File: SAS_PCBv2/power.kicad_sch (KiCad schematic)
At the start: 15 parts, among them J3 Conn_01x02_Pin, Q2 AO3401A, Q3 AO3401A, SW1 SW_SPST, U2 LF33_TO220

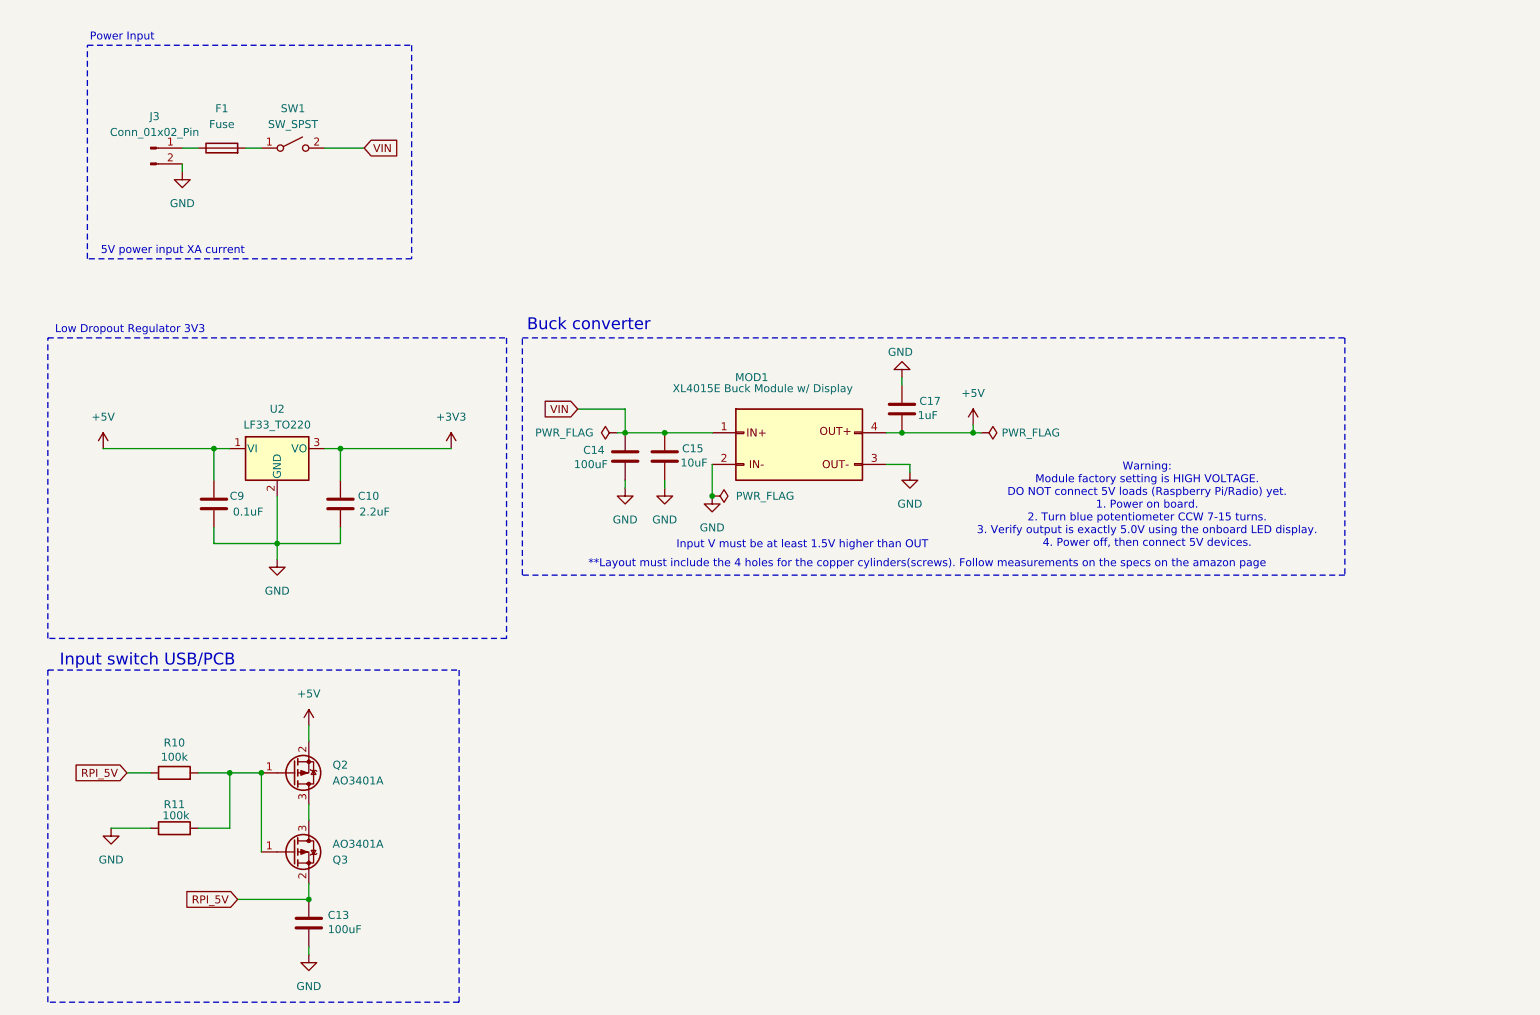
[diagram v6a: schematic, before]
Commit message: Amélioration des modèles Rpi et page power, switch PCB/USB fonctionnelle
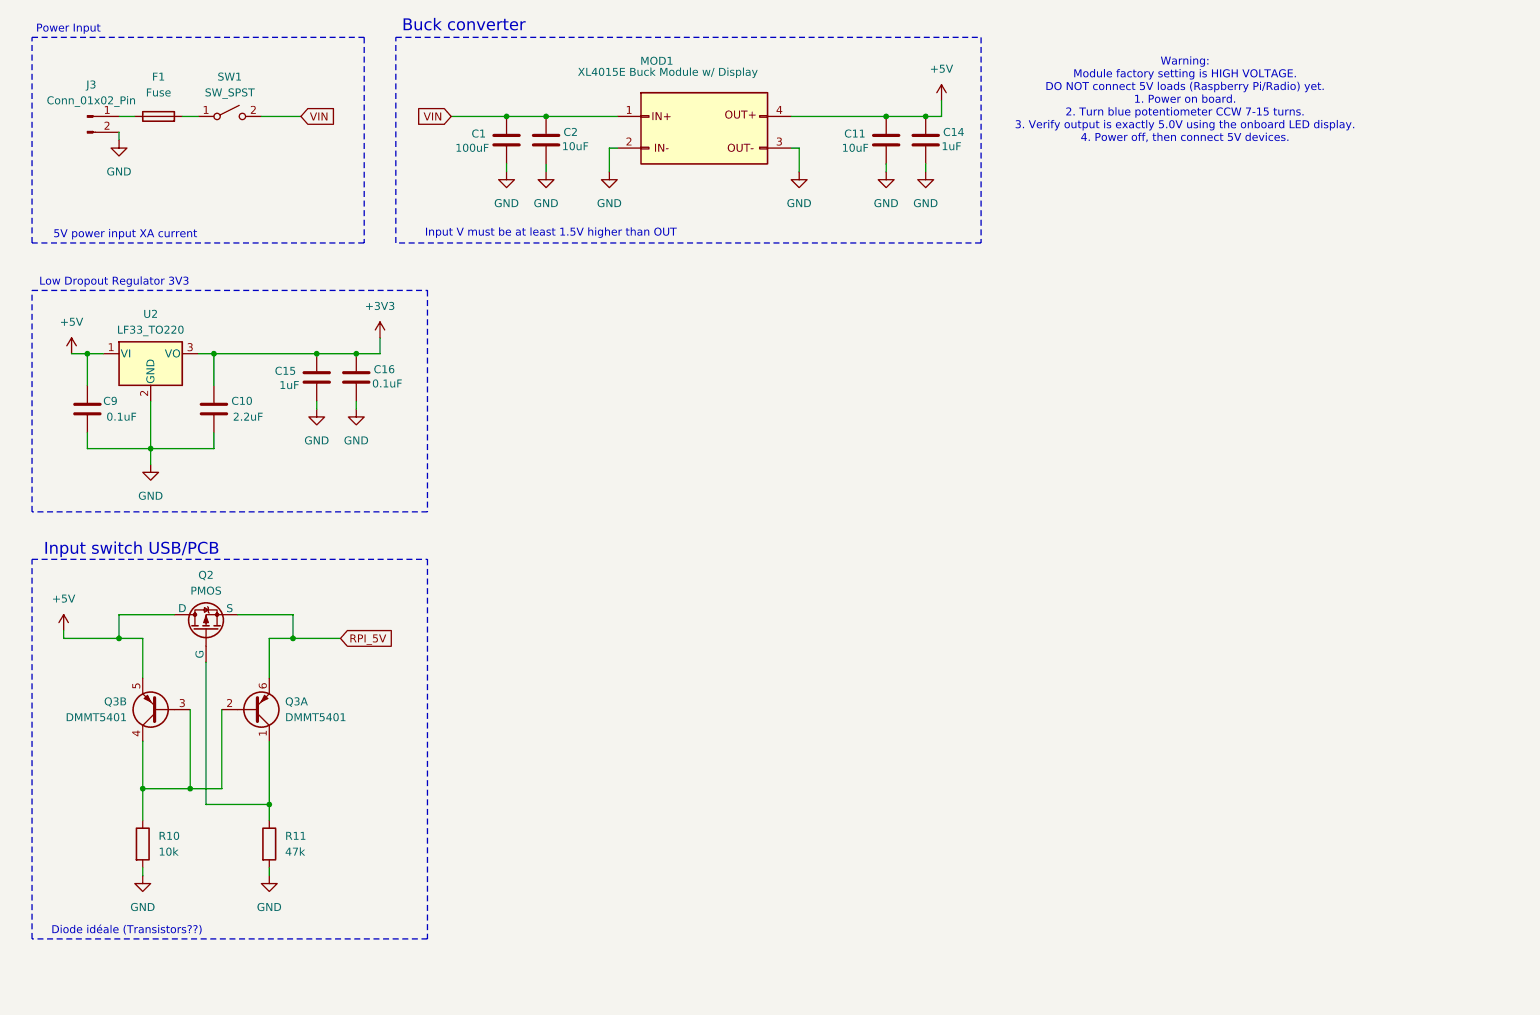
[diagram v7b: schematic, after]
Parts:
- removed C13: 100uF, symbol Device:C
- removed C17: 1uF, symbol Device:C
- removed Q2, Q3: AO3401A, Package_TO_SOT_SMD:SOT-23, symbol Transistor_FET:AO3401A
- added C1: 100uF, symbol Device:C
- added C11, C2: 10uF, symbol Device:C
- added C16: 0.1uF, symbol Device:C
- added Q2: PMOS, symbol Simulation_SPICE:PMOS
- added Q3: DMMT5401, Package_TO_SOT_SMD:SOT-23-6, symbol Transistor_BJT:DMMT5401
- C14: value 100uF -> 1uF
- C15: value 10uF -> 1uF
- R10: value 100k -> 10k
- R11: value 100k -> 47k
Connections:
- net +3V3: now also C15.1, C16.1
- net +5V: now also C14.1, C11.1, Q2.1 (D), Q3.5 (E2)
- net GND: now also R10.2, R11.2, C1.2, C11.2, C16.2, C2.2; no longer R11.1
- net RPI_5V: now also Q2.3 (S), Q3.6 (E1); no longer R10.1
- net VIN: now also C1.1, C2.1; no longer C14.1, C15.1
- new net: Q3.2 (B1), Q3.3 (B2), Q3.4 (C2), R10.1
- new net: Q2.2 (G), Q3.1 (C1), R11.1
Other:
- note added: "Diode idéale (Transistors??)"
- note removed: "**Layout must include the 4 holes for the copper cylinders(screws). Follow measurements on the specs on the amazon page"
- moved on the sheet: C10, C9, F1, J3, MOD1, SW1, U2

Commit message: Identification des transistors, footprint BMP280 et GPS Neo-6M, correction du fan PWM
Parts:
- removed Q2: PMOS, symbol Simulation_SPICE:PMOS
- removed Q3: DMMT5401, Package_TO_SOT_SMD:SOT-23-6, symbol Transistor_BJT:DMMT5401
- added MOSFET1: FQPF47P06, SAS_PCBv2_footprint:PMOS_FQP_ONS, symbol SAS_PCBv2_symbol:FQPF47P06
- added Q2, Q3: 2N4403, SAS_PCBv2_footprint:PBIP_2N4403_DIO, symbol Simulation_SPICE:PNP
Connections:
- net +5V: now also MOSFET1.2 (D), Q3.3 (E)
- net RPI_5V: now also MOSFET1.3 (S), Q2.3 (E)
- net at R10.1: now also Q2.2 (B), Q3.1 (C), Q3.2 (B)
- net at R11.1: now also MOSFET1.1 (G), Q2.1 (C)
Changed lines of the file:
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@@
-	)
-	(symbol
-		(lib_id "Transistor_BJT:DMMT5401")
-		(at 38.1 128.27 180)
-		(unit 2)
-		(exclude_from_sim no)
-		(in_bom yes)
-		(on_board yes)
-		(dnp no)
-		(fields_autoplaced yes)
-		(property "Reference" "Q3"
-			(at 33.02 126.9999 0)
-			(effects
-				(font
-					(size 1.27 1.27)
-				)
-				(justify left)
-			)
-		)
-		(property "Value" "DMMT5401"
-			(at 33.02 129.5399 0)
-			(effects
-				(font
-					(size 1.27 1.27)
-				)
-				(justify left)
-			)
-		)
-		(property "Footprint" "Package_TO_SOT_SMD:SOT-23-6"
-			(at 33.02 130.81 0)
-			(effects
-				(font
-					(size 1.27 1.27)
-				)
-				(hide yes)
-			)
-		)
-		(property "Datasheet" "https://www.diodes.com/assets/Datasheets/ds30437.pdf"
-			(at 38.1 128.27 0)
-			(effects
-				(font
-					(size 1.27 1.27)
-				)
-				(hide yes)
-			)
-		)
-		(property "Description" "Dual PNP transistor, 6 pin package"
-			(at 38.1 128.27 0)
-			(effects
-				(font
-					(size 1.27 1.27)
-				)
-				(hide yes)
-			)
-		)
-		(pin "4"
-		)
-		(pin "5"
-		)
-		(pin "6"
-		)
-		(pin "2"
-		)
-		(pin "3"
-		)
-		(pin "1"
-		)
-		(instances
-			(project ""
-				(path "/9d66b581-dc57-43dc-b827-73e5c0cd12f6/3d73fe98-5b95-4bdf-b7ce-5bce46366f48"
-					(reference "Q3")
-					(unit 2)
-				)
-			)
-		)
 	)
 	(symbol
@@
 	)
 	(symbol
+		(lib_id "Simulation_SPICE:PNP")
+		(at 38.1 128.27 180)
+		(unit 1)
+		(exclude_from_sim no)
+		(in_bom yes)
+		(on_board yes)
+		(dnp no)
+		(property "Reference" "Q3"
+			(at 33.02 126.9999 0)
+			(effects
+				(font
+					(size 1.27 1.27)
+				)
+				(justify left)
+			)
+		)
+		(property "Value" "2N4403"
+			(at 33.02 129.5399 0)
+			(effects
+				(font
+					(size 1.27 1.27)
+				)
+				(justify left)
+			)
+		)
+		(property "Footprint" "SAS_PCBv2_footprint:PBIP_2N4403_DIO"
+			(at 2.54 128.27 0)
+			(effects
+				(font
+					(size 1.27 1.27)
+				)
+				(hide yes)
+			)
+		)
+		(property "Datasheet" "https://diotec.com/request/datasheet/2n4403.pdf"
+			(at 2.54 128.27 0)
+			(effects
+				(font
+					(size 1.27 1.27)
+				)
+				(hide yes)
+			)
+		)
+		(property "Description" "2N4403"
+			(at 38.1 128.27 0)
+			(effects
+				(font
+					(size 1.27 1.27)
+				)
+				(hide yes)
+			)
+		)
+		(property "Sim.Device" "PNP"
+			(at 38.1 128.27 0)
+			(effects
+				(font
+					(size 1.27 1.27)
+				)
+				(hide yes)
+			)
+		)
+		(property "Sim.Type" "GUMMELPOON"
+			(at 38.1 128.27 0)
+			(effects
+				(font
+					(size 1.27 1.27)
+				)
+				(hide yes)
+			)
+		)
+		(property "Sim.Pins" "1=C 2=B 3=E"
+			(at 38.1 128.27 0)
+			(effects
+				(font
+					(size 1.27 1.27)
+				)
+				(hide yes)
+			)
+		)
+		(pin "3"
+		)
+		(pin "2"
+		)
+		(pin "1"
+		)
+		(instances
+			(project "SAS_PCBv2"
+				(path "/9d66b581-dc57-43dc-b827-73e5c0cd12f6/3d73fe98-5b95-4bdf-b7ce-5bce46366f48"
+					(reference "Q3")
+					(unit 1)
+				)
+			)
+		)
+	)
+	(symbol
 		(lib_id "power:GND")
 		(at 110.49 41.91 0)
@@
 	)
 	(symbol
-		(lib_id "Simulation_SPICE:PMOS")
-		(at 45.72 115.57 90)
-		(unit 1)
-		(exclude_from_sim no)
-		(in_bom yes)
-		(on_board yes)
-		(dnp no)
-		(fields_autoplaced yes)
-		(property "Reference" "Q2"
-			(at 45.72 106.68 90)
-			(effects
-				(font
-					(size 1.27 1.27)
-				)
-			)
-		)
-		(property "Value" "PMOS"
-			(at 45.72 109.22 90)
-			(effects
-				(font
-					(size 1.27 1.27)
-				)
-			)
-		)
-		(property "Footprint" ""
-			(at 43.18 110.49 0)
-			(effects
-				(font
-					(size 1.27 1.27)
-				)
-				(hide yes)
-			)
-		)
-		(property "Datasheet" "https://ngspice.sourceforge.io/docs/ngspice-html-manual/manual.xhtml#cha_MOSFETs"
-			(at 58.42 115.57 0)
-			(effects
-				(font
-					(size 1.27 1.27)
-				)
-				(hide yes)
-			)
-		)
-		(property "Description" "P-MOSFET transistor, drain/source/gate"
-			(at 45.72 115.57 0)
-			(effects
-				(font
-					(size 1.27 1.27)
-				)
-				(hide yes)
-			)
-		)
-		(property "Sim.Device" "PMOS"
-			(at 62.865 115.57 0)
-			(effects
-				(font
-					(size 1.27 1.27)
-				)
-				(hide yes)
-			)
-		)
-		(property "Sim.Type" "VDMOS"
-			(at 64.77 115.57 0)
-			(effects
-				(font
-					(size 1.27 1.27)
-				)
-				(hide yes)
-			)
-		)
-		(property "Sim.Pins" "1=D 2=G 3=S"
-			(at 60.96 115.57 0)
-			(effects
-				(font
-					(size 1.27 1.27)
-				)
-				(hide yes)
-			)
-		)
-		(pin "3"
-		)
-		(pin "1"
-		)
-		(pin "2"
-		)
-		(instances
-			(project ""
-				(path "/9d66b581-dc57-43dc-b827-73e5c0cd12f6/3d73fe98-5b95-4bdf-b7ce-5bce46366f48"
-					(reference "Q2")
-					(unit 1)
-				)
-			)
-		)
-	)
-	(symbol
 		(lib_id "power:+5V")
 		(at 24.13 71.12 0)
@@
 	)
 	(symbol
-		(lib_id "Transistor_BJT:DMMT5401")
+		(lib_id "Simulation_SPICE:PNP")
 		(at 53.34 128.27 0)
 		(mirror x)
@@
 		(dnp no)
 		(fields_autoplaced yes)
-		(property "Reference" "Q3"
+		(property "Reference" "Q2"
 			(at 58.42 126.9999 0)
 			(effects
@@
 			)
 		)
-		(property "Value" "DMMT5401"
+		(property "Value" "2N4403"
 			(at 58.42 129.5399 0)
 			(effects
@@
 			)
 		)
-		(property "Footprint" "Package_TO_SOT_SMD:SOT-23-6"
-			(at 58.42 130.81 0)
-			(effects
-				(font
-					(size 1.27 1.27)
-				)
-				(hide yes)
-			)
-		)
-		(property "Datasheet" "https://www.diodes.com/assets/Datasheets/ds30437.pdf"
+		(property "Footprint" "SAS_PCBv2_footprint:PBIP_2N4403_DIO"
+			(at 88.9 128.27 0)
+			(effects
+				(font
+					(size 1.27 1.27)
+				)
+				(hide yes)
+			)
+		)
+		(property "Datasheet" "https://diotec.com/request/datasheet/2n4403.pdf"
+			(at 88.9 128.27 0)
+			(effects
+				(font
+					(size 1.27 1.27)
+				)
+				(hide yes)
+			)
+		)
+		(property "Description" "2N4403"
 			(at 53.34 128.27 0)
 			(effects
@@
 			)
 		)
-		(property "Description" "Dual PNP transistor, 6 pin package"
+		(property "Sim.Device" "PNP"
 			(at 53.34 128.27 0)
 			(effects
@@
 			)
 		)
-		(pin "4"
-		)
-		(pin "5"
-		)
-		(pin "6"
+		(property "Sim.Type" "GUMMELPOON"
+			(at 53.34 128.27 0)
+			(effects
+				(font
+					(size 1.27 1.27)
+				)
+				(hide yes)
+			)
+		)
+		(property "Sim.Pins" "1=C 2=B 3=E"
+			(at 53.34 128.27 0)
+			(effects
+				(font
+					(size 1.27 1.27)
+				)
+				(hide yes)
+			)
+		)
+		(pin "3"
 		)
 		(pin "2"
 		)
-		(pin "3"
-		)
 		(pin "1"
 		)
@@
 			(project ""
 				(path "/9d66b581-dc57-43dc-b827-73e5c0cd12f6/3d73fe98-5b95-4bdf-b7ce-5bce46366f48"
-					(reference "Q3")
+					(reference "Q2")
 					(unit 1)
 				)
@@
 					(unit 1)
 				)
+			)
+		)
+	)
+	(symbol
+		(lib_id "SAS_PCBv2_symbol:FQPF47P06")
+		(at 45.72 120.65 90)
+		(unit 1)
+		(exclude_from_sim no)
+		(in_bom yes)
+		(on_board yes)
+		(dnp no)
+		(property "Reference" "MOSFET1"
+			(at 45.974 106.426 90)
+			(effects
+				(font
+					(size 1.524 1.524)
+				)
+				(hide yes)
+			)
+		)
+		(property "Value" "FQPF47P06"
+			(at 45.72 108.966 90)
+			(effects
+				(font
+					(size 1.524 1.524)
+				)
+			)
+		)
+		(property "Footprint" "SAS_PCBv2_footprint:PMOS_FQP_ONS"
+			(at 45.72 120.65 0)
+			(effects
+				(font
+					(size 1.27 1.27)
+					(italic yes)
+				)
+				(hide yes)
+			)
+		)
+		(property "Datasheet" "https://www.onsemi.com/pdf/datasheet/fqpf47p06-d.pdf"
+			(at 45.72 120.65 0)
+			(effects
+				(font
+					(size 1.27 1.27)
+					(italic yes)
+				)
+				(hide yes)
+			)
+		)
+		(property "Description" "FQPF47P06FS"
+			(at 45.72 120.65 0)
+			(effects
+				(font
+					(size 1.27 1.27)
+				)
+				(hide yes)
+			)
+		)
+		(pin "2"
+		)
+		(pin "1"
+		)
+		(pin "3"
+		)
+		(instances
+			(project ""
+				(path "/9d66b581-dc57-43dc-b827-73e5c0cd12f6/3d73fe98-5b95-4bdf-b7ce-5bce46366f48"
+					(reference "MOSFET1")
+					(unit 1)
+				)
